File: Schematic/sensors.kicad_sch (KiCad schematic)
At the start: 17 parts, among them IC4 ICM-42688-P, IC5 MPU-6500, U5 SPL06-001, U7 QMC5883L

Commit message: Refactor code structure for improved readability and maintainability
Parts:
- removed IC4: ICM-42688-P, fch7_fp:LGA-16_L3.0-W3.0-P0.50-BL_SQ, symbol ICM-42688-P:ICM-42688-P
- removed IC5: MPU-6500, fch7_fp:QFN40P300X300X95-25M-D, symbol MPU-6500:MPU-6500
- removed U7: QMC5883L, fch7_fp:LGA-16_L3.0-W3.0-P0.50-BL_SQ, symbol fclib:QMC5883L
- added IC4: ICM-42688-P, fch7_fp:IIM42352, symbol fclib:ICM-42688-P
- added IC5: MPU-6500, fch7_fp:QFN40P300X300X95-25M-D, symbol fclib:MPU-6500
- added U4: QMC5883L, fch7_fp:LGA-16_L3.0-W3.0-P0.50-BL_SQ, symbol fclib:QMC5883L
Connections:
- net GND: now also IC4.10 (RESV_4), IC4.11 (RESV_5), IC4.2 (RESV_1), IC4.3 (RESV_2), IC4.6 (GND), IC4.7 (RESV_3), IC4.9 (INT2_/_FSYNC_/_CLKIN), IC5.18 (GND_1), IC5.19 (RESV_1), IC5.25 (GND_2), U4.14 (GND), U4.16 (GND)
- net I2C1_CLK: now also U4.1 (SCL)
- net I2C1_SDA: now also U4.9 (SDA)
- net IMU1_SPI4_EXTI2: now also IC4.4 (INT1_/_INT)
- net IMU2_SPI1_EXTI1: now also IC5.12 (INT)
- net SPI1_IMU1_CS: now also IC5.22 (NCS)
- net SPI1_MISO: now also IC5.9 (SDO_/_AD0)
- net SPI1_MOSI: now also IC5.24 (SDA_/_SDI)
- net SPI1_SCLK: now also IC5.23 (SCL_/_SCLK)
- net SPI4_IMU2_CS: now also IC4.12 (AP_CS)
- net SPI4_MISO: now also IC4.1 (AP_SDO_/_AP_AD0)
- net SPI4_MOSI: now also IC4.14 (AP_SDA_/_AP_SDIO_/_AP_SDI)
- net SPI4_SCLK: now also IC4.13 (AP_SCL_/_AP_SCLK)
- net VCC_ICM: now also IC4.5 (VDDIO), IC4.8 (VDD)
- net VDD_MCU: now also IC5.13 (VDD), IC5.8 (VDDIO), U4.12 (VDDIO), U4.2 (VDD), U4.4 (S1)
- net at C32.2: now also IC5.10 (REGOUT)
- net at C38.2: now also U4.13 (SETC)
- net at C39.1: now also U4.15 (C1)
- net at C38.1: now also U4.8 (SETP)

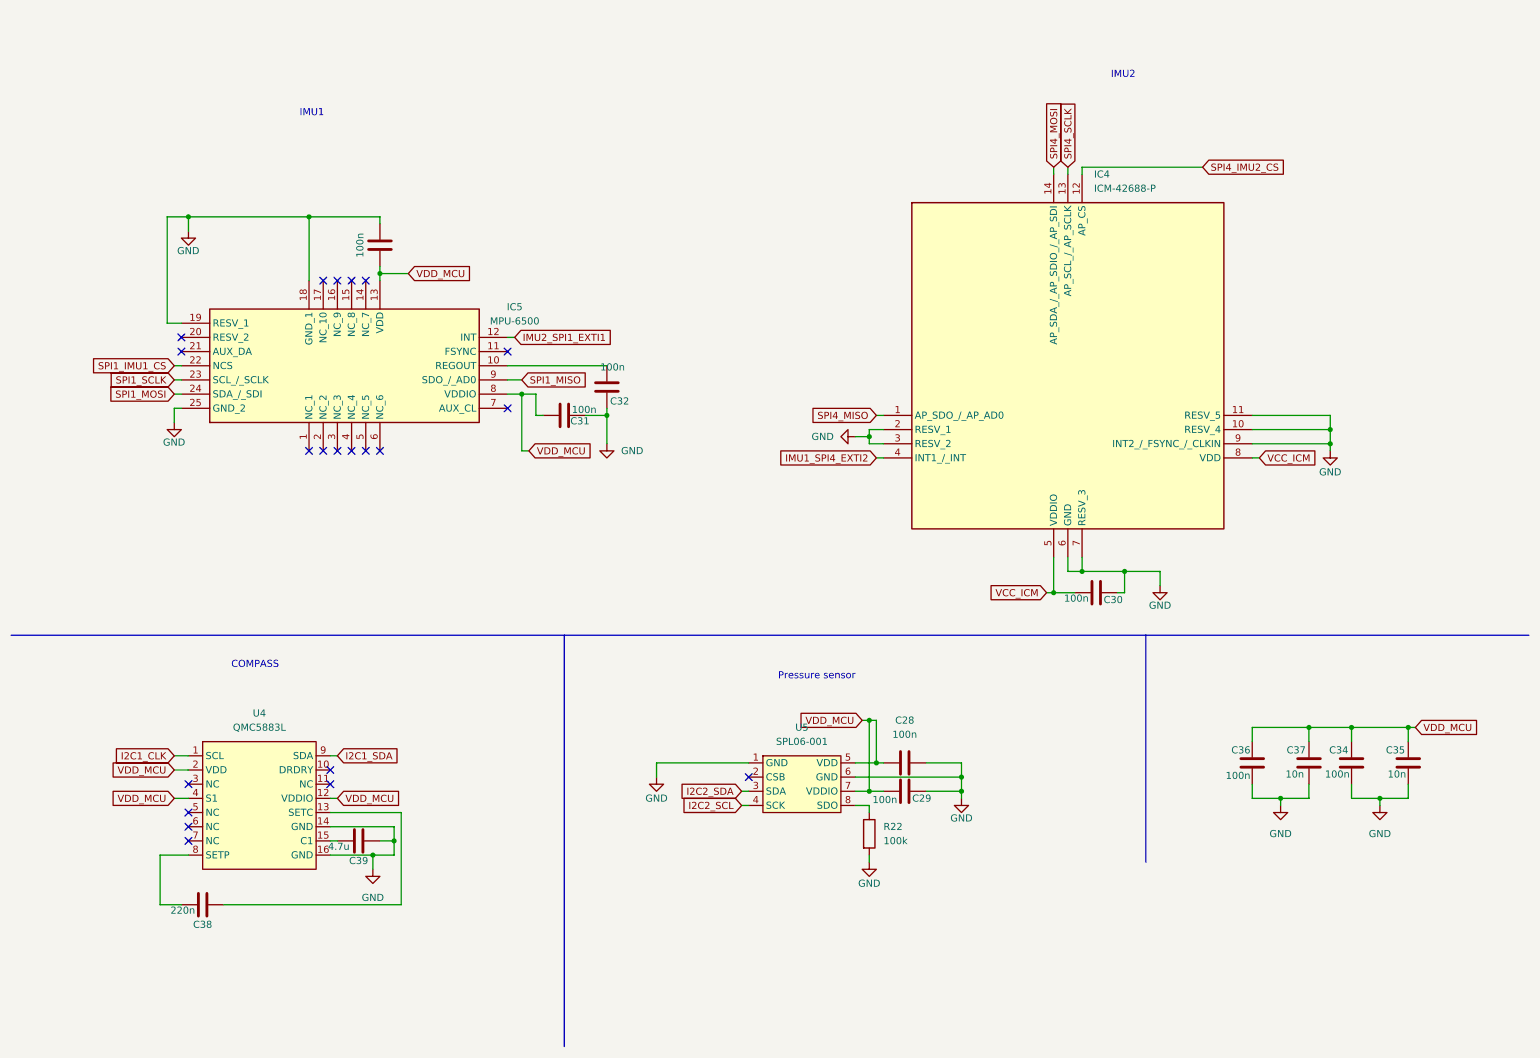
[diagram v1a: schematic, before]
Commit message: Refactor schematic files and add net definitions
- Updated priority values for GND and POWER net classes in fch7.kicad_pro.
- Added USB_DIFF net class with associated patterns for USB differential signals.
- Removed duplicate junctions and adjusted wire connections in rf_rx.kicad_sch for clarity.
- Adjusted component positions and properties in rf_rx.kicad_sch for better layout.
- Modified text positions for IMU components in sensors.kicad_sch to improve readability.
- Cleaned up unnecessary wires and added new connections in sensors.kicad_sch.
- Introduced nets.txt file to define various electrical nets used across the schematics.
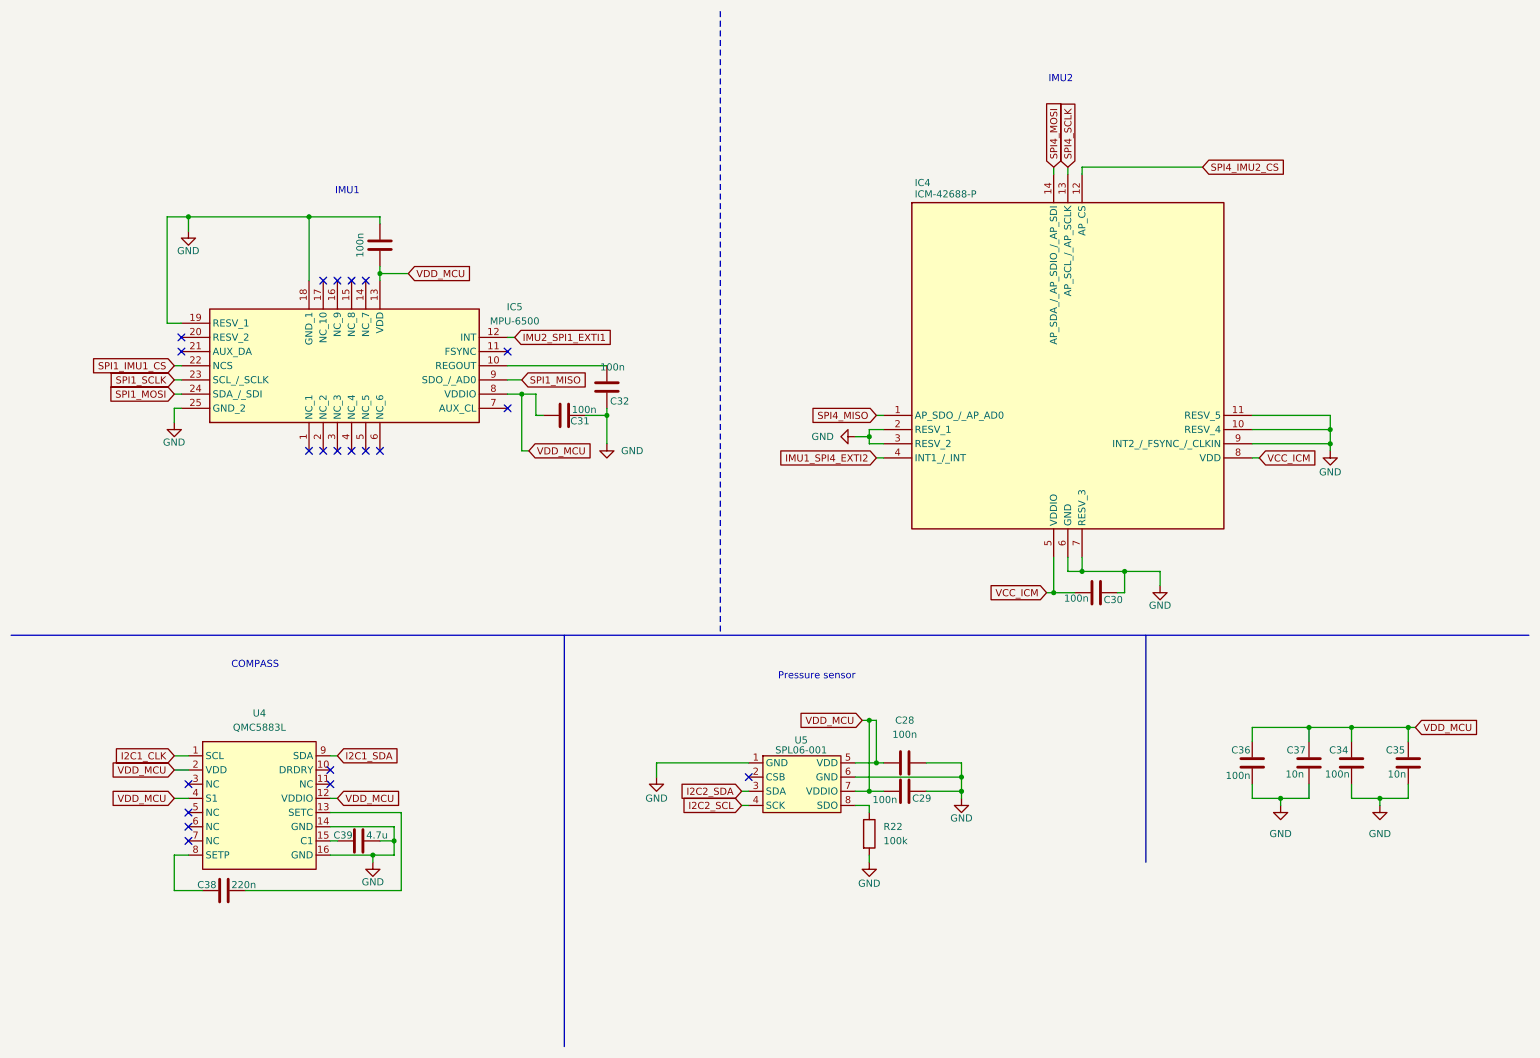
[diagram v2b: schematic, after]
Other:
- moved on the sheet: C38
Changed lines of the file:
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@@
 	(text "IMU2\n"
 		(exclude_from_sim no)
-		(at 211.836 24.13 0)
+		(at 200.66 24.892 0)
 		(effects
 			(font
@@
 	(text "IMU1\n"
 		(exclude_from_sim no)
-		(at 66.548 30.988 0)
+		(at 72.898 44.958 0)
 		(effects
 			(font
@@
 	(wire
 		(pts
-			(xy 82.55 172.72) (xy 50.8 172.72)
-		)
-		(stroke
-			(width 0)
-			(type default)
-		)
-	)
-	(wire
-		(pts
 			(xy 198.12 116.84) (xy 199.39 116.84)
 		)
@@
 	(wire
 		(pts
+			(xy 77.47 163.83) (xy 77.47 165.1)
+		)
+		(stroke
+			(width 0)
+			(type default)
+		)
+	)
+	(wire
+		(pts
 			(xy 41.91 76.2) (xy 43.18 76.2)
 		)
@@
 	(wire
 		(pts
-			(xy 143.51 152.4) (xy 144.78 152.4)
+			(xy 77.47 163.83) (xy 81.28 163.83)
 		)
 		(stroke
@@
 	(wire
 		(pts
-			(xy 39.37 172.72) (xy 43.18 172.72)
+			(xy 143.51 152.4) (xy 144.78 152.4)
 		)
 		(stroke
@@
 	(wire
 		(pts
+			(xy 82.55 170.18) (xy 82.55 156.21)
+		)
+		(stroke
+			(width 0)
+			(type default)
+		)
+	)
+	(wire
+		(pts
 			(xy 69.85 158.75) (xy 81.28 158.75)
 		)
@@
 	(wire
 		(pts
-			(xy 77.47 163.83) (xy 77.47 166.37)
+			(xy 43.18 68.58) (xy 40.64 68.58)
 		)
 		(stroke
@@
 	(wire
 		(pts
-			(xy 43.18 68.58) (xy 40.64 68.58)
+			(xy 199.39 40.64) (xy 199.39 41.91)
 		)
 		(stroke
@@
 	(wire
 		(pts
-			(xy 199.39 40.64) (xy 199.39 41.91)
+			(xy 167.64 147.32) (xy 168.91 147.32)
 		)
 		(stroke
@@
 	(wire
 		(pts
-			(xy 167.64 147.32) (xy 168.91 147.32)
+			(xy 43.18 83.82) (xy 41.91 83.82)
 		)
 		(stroke
@@
 		)
 	)
-	(wire
+	(polyline
 		(pts
-			(xy 43.18 83.82) (xy 41.91 83.82)
+			(xy 139.7 12.7) (xy 139.7 124.46)
 		)
 		(stroke
 			(width 0)
-			(type default)
+			(type dash)
 		)
 	)
@@
 	(wire
 		(pts
+			(xy 54.61 170.18) (xy 82.55 170.18)
+		)
+		(stroke
+			(width 0)
+			(type default)
+		)
+	)
+	(wire
+		(pts
 			(xy 107.95 85.09) (xy 106.68 85.09)
 		)
@@
 	(wire
 		(pts
-			(xy 262.89 153.67) (xy 257.81 153.67)
+			(xy 41.91 163.83) (xy 44.45 163.83)
 		)
 		(stroke
@@
 	(wire
 		(pts
-			(xy 39.37 163.83) (xy 39.37 172.72)
+			(xy 262.89 153.67) (xy 257.81 153.67)
+		)
+		(stroke
+			(width 0)
+			(type default)
+		)
+	)
+	(polyline
+		(pts
+			(xy 12.7 124.46) (xy 284.48 124.46)
 		)
 		(stroke
@@
 	(wire
 		(pts
-			(xy 83.82 59.69) (xy 78.74 59.69)
+			(xy 41.91 170.18) (xy 41.91 163.83)
 		)
 		(stroke
@@
 	(wire
 		(pts
-			(xy 176.53 152.4) (xy 182.88 152.4)
+			(xy 83.82 59.69) (xy 78.74 59.69)
 		)
 		(stroke
@@
 	(wire
 		(pts
-			(xy 212.09 113.03) (xy 212.09 116.84)
+			(xy 176.53 152.4) (xy 182.88 152.4)
 		)
 		(stroke
@@
 		)
 	)
-	(polyline
+	(wire
 		(pts
-			(xy 12.7 124.46) (xy 215.9 124.46)
+			(xy 212.09 113.03) (xy 212.09 116.84)
 		)
 		(stroke
@@
 	(wire
 		(pts
-			(xy 81.28 158.75) (xy 81.28 161.29)
+			(xy 46.99 170.18) (xy 41.91 170.18)
 		)
 		(stroke
@@
 	(wire
 		(pts
-			(xy 204.47 110.49) (xy 204.47 113.03)
+			(xy 81.28 158.75) (xy 81.28 161.29)
 		)
 		(stroke
@@
 		)
 	)
-	(polyline
+	(wire
 		(pts
-			(xy 284.48 124.46) (xy 215.9 124.46)
+			(xy 204.47 110.49) (xy 204.47 113.03)
 		)
 		(stroke
@@
 	(wire
 		(pts
-			(xy 82.55 156.21) (xy 82.55 172.72)
-		)
-		(stroke
-			(width 0)
-			(type default)
-		)
-	)
-	(wire
-		(pts
 			(xy 234.95 90.17) (xy 248.92 90.17)
 		)
@@
 	(wire
 		(pts
-			(xy 81.28 163.83) (xy 77.47 163.83)
-		)
-		(stroke
-			(width 0)
-			(type default)
-		)
-	)
-	(wire
-		(pts
 			(xy 166.37 139.7) (xy 167.64 139.7)
 		)
@@
 	(wire
 		(pts
-			(xy 44.45 163.83) (xy 39.37 163.83)
-		)
-		(stroke
-			(width 0)
-			(type default)
-		)
-	)
-	(wire
-		(pts
 			(xy 204.47 113.03) (xy 212.09 113.03)
 		)
@@
 		(on_board yes)
 		(dnp no)
-		(fields_autoplaced yes)
 		(property "Reference" "IC4"
-			(at 206.6133 41.91 0)
+			(at 174.498 43.434 0)
 			(effects
 				(font
@@
 		)
 		(property "Value" "ICM-42688-P"
-			(at 206.6133 44.45 0)
+			(at 174.498 45.466 0)
 			(effects
 				(font
@@
 	(symbol
 		(lib_id "Device:C")
-		(at 46.99 172.72 90)
+		(at 50.8 170.18 90)
 		(unit 1)
 		(exclude_from_sim no)
@@
 		(dnp no)
 		(property "Reference" "C38"
-			(at 46.99 176.276 90)
+			(at 47.752 169.164 90)
 			(effects
 				(font
@@
 		)
 		(property "Value" "220n"
-			(at 43.434 173.736 90)
+			(at 54.356 169.164 90)
 			(effects
 				(font
@@
 		)
 		(property "Footprint" "Capacitor_SMD:C_0603_1608Metric"
-			(at 50.8 171.7548 0)
+			(at 54.61 169.2148 0)
 			(effects
 				(font
@@
 		)
 		(property "Datasheet" "https://www.lcsc.com/datasheet/C83626.pdf"
-			(at 46.99 172.72 0)
+			(at 50.8 170.18 0)
 			(effects
 				(font
@@
 		)
 		(property "Description" "Unpolarized capacitor"
-			(at 46.99 172.72 0)
+			(at 50.8 170.18 0)
 			(effects
 				(font
@@
 		)
 		(property "Fréquence" ""
-			(at 46.99 172.72 90)
+			(at 50.8 170.18 90)
 			(effects
 				(font
@@
 		)
 		(property "MPN" "0603B224K500NT"
-			(at 46.99 172.72 90)
+			(at 50.8 170.18 90)
 			(effects
 				(font
@@
 		)
 		(property "Manufacturer" "FH"
-			(at 46.99 172.72 90)
+			(at 50.8 170.18 90)
 			(effects
 				(font
@@
 		(dnp no)
 		(property "Reference" "C39"
-			(at 74.93 164.846 90)
+			(at 72.136 160.274 90)
 			(effects
 				(font
@@
 		)
 		(property "Value" "4.7u"
-			(at 71.374 162.306 90)
+			(at 78.232 160.274 90)
 			(effects
 				(font
@@
 	(symbol
 		(lib_id "power:GND")
-		(at 77.47 166.37 0)
+		(at 77.47 165.1 0)
 		(unit 1)
 		(exclude_from_sim no)
@@
 		(on_board yes)
 		(dnp no)
-		(fields_autoplaced yes)
 		(property "Reference" "#PWR032"
-			(at 77.47 172.72 0)
+			(at 77.47 171.45 0)
 			(effects
 				(font
@@
 		)
 		(property "Value" "GND"
-			(at 77.47 171.45 0)
+			(at 77.47 168.656 0)
 			(effects
 				(font
@@
 		)
 		(property "Footprint" ""
-			(at 77.47 166.37 0)
+			(at 77.47 165.1 0)
 			(effects
 				(font
@@
 		)
 		(property "Datasheet" ""
-			(at 77.47 166.37 0)
+			(at 77.47 165.1 0)
 			(effects
 				(font
@@
 		)
 		(property "Description" "Power symbol creates a global label with name \"GND\" , ground"
-			(at 77.47 166.37 0)
+			(at 77.47 165.1 0)
 			(effects
 				(font
@@
 		(on_board yes)
 		(dnp no)
-		(fields_autoplaced yes)
 		(property "Reference" "U5"
-			(at 154.305 140.97 0)
+			(at 154.178 143.256 0)
 			(effects
 				(font
@@
 		)
 		(property "Value" "SPL06-001"
-			(at 154.305 143.51 0)
+			(at 154.178 145.034 0)
 			(effects
 				(font

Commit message: finished every routing and fix errors in DRC
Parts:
- IC4: footprint fch7_fp:IIM42352 -> fch7:IIM42352
- IC5: footprint fch7_fp:QFN40P300X300X95-25M-D -> fch7:QFN40P300X300X95-25M-D
- U4: footprint fch7_fp:LGA-16_L3.0-W3.0-P0.50-BL_SQ -> fch7:LGA-16_L3.0-W3.0-P0.50-BL_SQ
- U5: footprint fch7_fp:SENSOR-SMD_SPL06-001 -> fch7:SENSOR-SMD_SPL06-001
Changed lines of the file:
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@@
 			)
 		)
-		(property "Footprint" "fch7_fp:IIM42352"
+		(property "Footprint" "fch7:IIM42352"
 			(at 231.14 144.45 0)
 			(effects
@@
 			)
 		)
-		(property "Footprint" "fch7_fp:LGA-16_L3.0-W3.0-P0.50-BL_SQ"
+		(property "Footprint" "fch7:LGA-16_L3.0-W3.0-P0.50-BL_SQ"
 			(at 57.15 154.94 0)
 			(effects
@@
 			)
 		)
-		(property "Footprint" "fch7_fp:SENSOR-SMD_SPL06-001"
+		(property "Footprint" "fch7:SENSOR-SMD_SPL06-001"
 			(at 153.67 151.13 0)
 			(effects
@@
 			)
 		)
-		(property "Footprint" "fch7_fp:QFN40P300X300X95-25M-D"
+		(property "Footprint" "fch7:QFN40P300X300X95-25M-D"
 			(at 145.72 64.77 0)
 			(effects

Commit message: Update schematic properties and model paths - Added MPN and Manufacturer properties for ICM-42688-P and MPU-6500 in sensors.kicad_sch. - Changed model paths to use the ${FCH7_3DMODEL_DIR} variable for various components in the fch7.pretty library. - Added a 3D model for the SOD-123 component.
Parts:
- IC4: MPN (none) -> ICM-42688-P; Manufacturer (none) -> TDK
- IC5: MPN (none) -> MPU-6500; Manufacturer (none) -> TDK
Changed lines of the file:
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@@
+			)
+		)
+		(property "MPN" "ICM-42688-P"
+			(at 168.91 85.09 0)
+			(effects
+				(font
+					(size 1.27 1.27)
+				)
+				(hide yes)
+			)
+		)
+		(property "Manufacturer" "TDK"
+			(at 168.91 85.09 0)
+			(effects
+				(font
+					(size 1.27 1.27)
+				)
+				(hide yes)
 			)
 		)
@@
 				(hide yes)
 			)
+		)
+		(property "MPN" "MPU-6500"
+			(at 66.04 91.44 90)
+			(effects
+				(font
+					(size 1.27 1.27)
+				)
+				(hide yes)
+			)
+		)
+		(property "Manufacturer" "TDK"
+			(at 66.04 91.44 90)
+			(effects
+				(font
+					(size 1.27 1.27)
+				)
+				(hide yes)
+			)
